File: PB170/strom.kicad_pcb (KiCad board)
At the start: 4 copper layers, 121.9 x 94 mm, 39 parts, among them J1 USB_B_Micro-Connector, SW1 Switch_SW_MEC_5E, U1 74HC74, U10 74HC08, U11 74HC08, U12 74HC08, U13 74HC08, U14 74HC08, U15 74HC08, U16 NE555D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

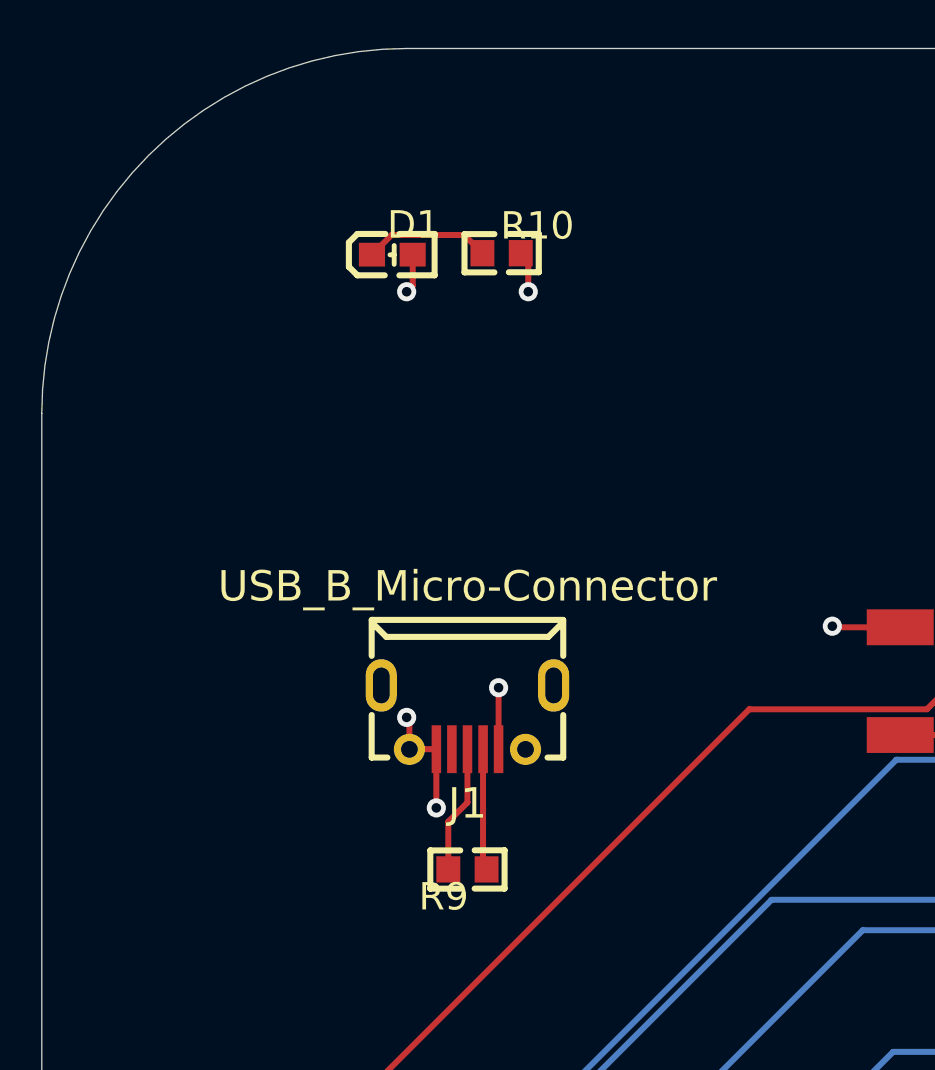
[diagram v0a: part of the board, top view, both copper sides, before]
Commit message: changed USB position in PCB
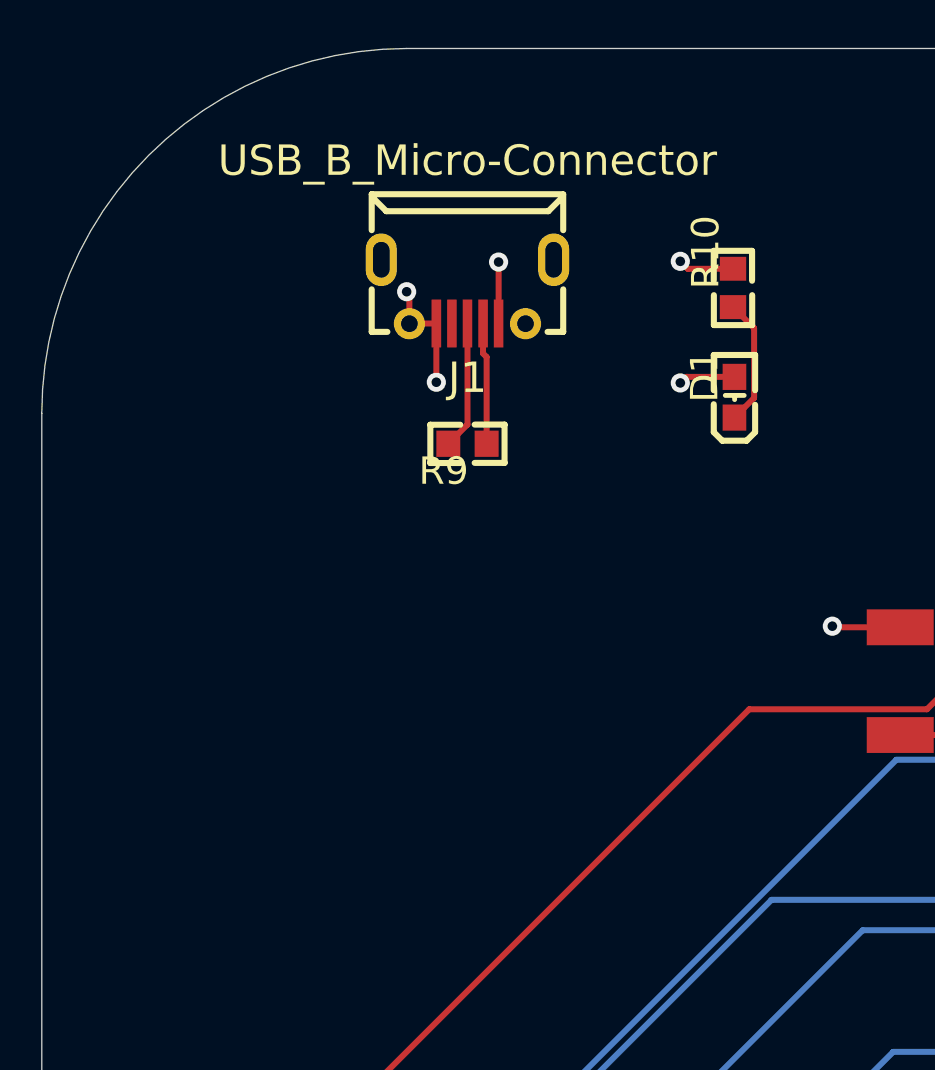
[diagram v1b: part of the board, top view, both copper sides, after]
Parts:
- moved J1 17.8 mm to (72.4, 39.4)
- moved R9 17.8 mm to (72.4, 45.7)
- moved D1 15.5 mm to (83.5, 43.8), turned to 90 degrees
- moved R10 9.77 mm to (83.5, 39.2), turned to 90 degrees
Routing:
- net GND: track 450.4 -> 458.4 mm
- net VCC: track 430.7 -> 429.9 mm

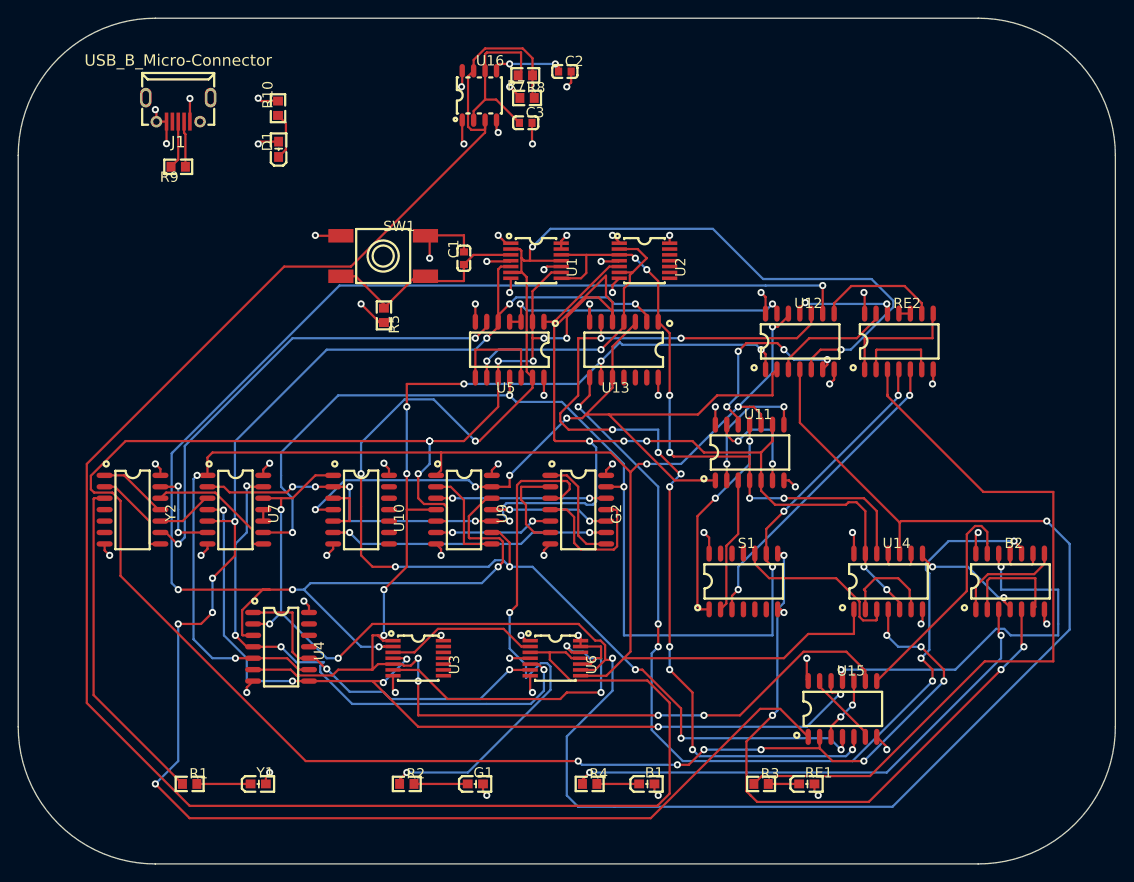
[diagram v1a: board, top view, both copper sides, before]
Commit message: Changed button position
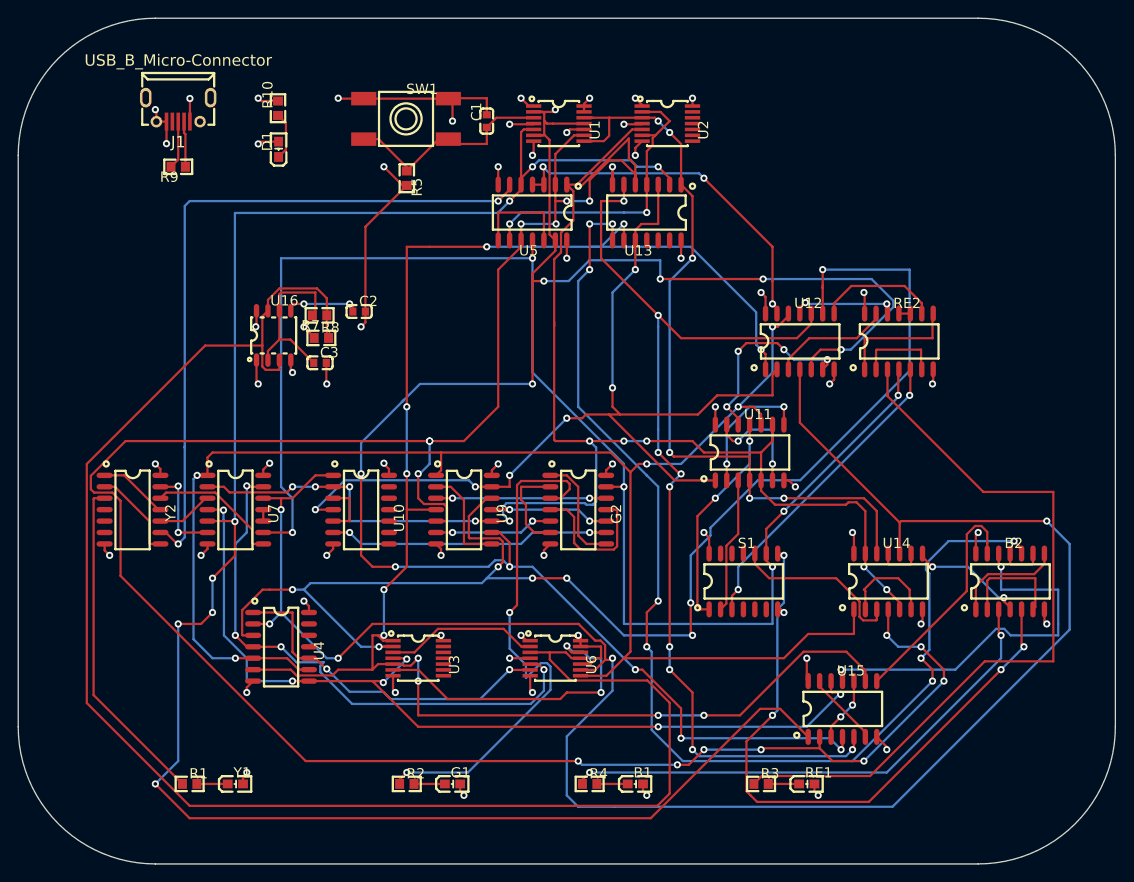
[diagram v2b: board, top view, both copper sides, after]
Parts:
- moved C2 35.1 mm to (92.5, 61.8)
- moved R8 35.1 mm to (88.3, 64.7)
- moved C3 35.1 mm to (88.1, 67.5)
- moved R7 35.1 mm to (88.1, 62.2)
- moved U16 35.1 mm to (83.0, 64.5)
- moved U5 15.5 mm to (111.8, 50.8)
- moved U13 15.5 mm to (124.5, 50.8)
- moved C1 15.5 mm to (106.7, 40.6)
- moved U1 15.5 mm to (114.7, 40.9)
- moved SW1 15.5 mm to (97.7, 40.4)
- moved U2 15.5 mm to (126.7, 40.9)
- moved R5 15.5 mm to (97.8, 47.0)
- moved Y1 2.54 mm to (78.7, 114.3)
- moved G1 2.54 mm to (102.9, 114.3)
- moved B1 1.27 mm to (123.2, 114.3)
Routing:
- net Net-(R7-Pad1): track 212.7 -> 176.7 mm
- net /blue/I1I2I3: track 132.0 -> 162.2 mm
- net /blue/Q1Q2: track 165.6 -> 190.3 mm
- net /button/I1I2I3: track 53.3 -> 78.0 mm
- net /blue/I3: track 188.9 -> 212.6 mm
- net Net-(B2-Pad10): track 106.7 -> 128.6 mm, vias 6 -> 8
- net /blue/I2: track 242.1 -> 260.2 mm
- net /blue/I1: track 138.4 -> 155.3 mm
- net /blue/nI2I3: track 89.9 -> 106.7 mm, vias 4 -> 6
- net /blue/nI2: track 71.7 -> 88.0 mm
- net /flipflops/nQ1Q2: track 169.0 -> 154.1 mm, vias 5 -> 8
- net /blue/nI3: track 192.7 -> 206.7 mm, vias 9 -> 12
- net GND: track 458.4 -> 447.5 mm
- net /button/I1I2: track 33.3 -> 40.2 mm, vias 2 -> 3
- net VCC: track 429.9 -> 424.7 mm
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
